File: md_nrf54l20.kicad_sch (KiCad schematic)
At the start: 49 parts, among them J10 Conn_01x15, J2 Conn_01x04, J5 USB_C, J7 JST SH I2C, J9 Conn_01x15, SW1 RESET, U1 nRF54L20, U3 CH347T, U4 AP2112K-3.3, U5 MLD-TF PUSH-H18, Y1 8MHz, Y2 32MHz

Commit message: Fixing Digital mapping
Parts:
- added D6: G_LED, LED_SMD:LED_0402_1005Metric, symbol Device:LED
- added R17: 220, Resistor_SMD:R_0402_1005Metric, symbol Device:R
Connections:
- net +3V3: now also R17.2
- net D10_CS: now also U1.11 (P1.01)
- net D8: now also U1.28 (P0.07)
- net at U1.3 (P2.03): now also D6.1 (K)
- new net: D6.2 (A), R17.1
- no-connect marks 17 -> 18
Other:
- moved on the sheet: C2, C3, C4, C7, C8, R1, R13, R14, R15, R16, SW1, U5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

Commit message: Fixing Digital mapping
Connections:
- net D0_RX: no longer U1.49 (P1.21)
- net D13_SCK: now also U1.26 (P0.04); no longer U1.50 (P1.24)
- net D3_PWM: no longer U1.12 (P1.02)
- net D4: now also U1.3 (P2.03); no longer U1.29 (P0.08)
- net D6_PWM: no longer U1.41 (P1.18)
- net D8: no longer U1.28 (P0.07)
- net at D6.1 (K): no longer U1.3 (P2.03)
- no-connect marks 18 -> 17
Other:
- moved on the sheet: D6, R17
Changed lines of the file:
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@@
 	)
 	(no_connect
-		(at 444.5 217.17)
-	)
-	(no_connect
 		(at 259.08 208.28)
 	)
@@
 	(wire
 		(pts
-			(xy 471.17 240.03) (xy 430.53 240.03)
-		)
-		(stroke
-			(width 0)
-			(type default)
-		)
-	)
-	(wire
-		(pts
 			(xy 383.54 264.16) (xy 394.97 264.16)
 		)
@@
 	(wire
 		(pts
+			(xy 430.53 240.03) (xy 438.15 240.03)
+		)
+		(stroke
+			(width 0)
+			(type default)
+		)
+	)
+	(wire
+		(pts
 			(xy 411.48 144.78) (xy 411.48 208.28)
 		)
@@
 	(wire
 		(pts
-			(xy 485.14 240.03) (xy 478.79 240.03)
+			(xy 505.46 207.01) (xy 499.11 207.01)
 		)
 		(stroke
@@
 		)
 	)
-	(label "D4"
-		(at 448.31 226.06 180)
-		(effects
-			(font
-				(size 1.27 1.27)
-			)
-			(justify right bottom)
-		)
-	)
 	(label "SWDCLK"
 		(at 337.82 306.07 180)
@@
 		)
 	)
-	(label "D3_PWM"
-		(at 379.73 219.71 0)
-		(effects
-			(font
-				(size 1.27 1.27)
-			)
-			(justify left bottom)
-		)
-	)
 	(label "SD_CS"
 		(at 641.35 152.4 0)
@@
 		)
 	)
-	(label "D8"
-		(at 448.31 223.52 180)
+	(label "D0_RX"
+		(at 370.84 243.84 0)
 		(effects
 			(font
 				(size 1.27 1.27)
 			)
-			(justify right bottom)
+			(justify left bottom)
 		)
 	)
@@
 		)
 	)
+	(label "D4"
+		(at 438.15 240.03 180)
+		(effects
+			(font
+				(size 1.27 1.27)
+			)
+			(justify right bottom)
+		)
+	)
 	(label "CH_UART_RX"
 		(at 342.9 298.45 180)
@@
 		)
 	)
+	(label "D8"
+		(at 372.11 257.81 180)
+		(effects
+			(font
+				(size 1.27 1.27)
+			)
+			(justify right bottom)
+		)
+	)
 	(label "A3"
 		(at 383.54 266.7 0)
@@
 		)
 	)
+	(label "D3_PWM"
+		(at 369.57 237.49 0)
+		(effects
+			(font
+				(size 1.27 1.27)
+			)
+			(justify left bottom)
+		)
+	)
 	(label "D2"
 		(at 379.73 237.49 0)
@@
 		)
 	)
+	(label "D6_PWM"
+		(at 363.22 252.73 0)
+		(effects
+			(font
+				(size 1.27 1.27)
+			)
+			(justify left bottom)
+		)
+	)
 	(label "D12_CITO"
 		(at 466.09 349.25 180)
@@
 		)
 	)
-	(label "D6_PWM"
-		(at 379.73 247.65 0)
-		(effects
-			(font
-				(size 1.27 1.27)
-			)
-			(justify left bottom)
-		)
-	)
 	(label "SD_SCK"
 		(at 439.42 234.95 180)
@@
 		)
 	)
-	(label "A6"
-		(at 389.89 336.55 180)
+	(label "D13_SCK"
+		(at 444.5 217.17 180)
 		(effects
 			(font
@@
 		)
 	)
-	(label "D0_RX"
-		(at 372.11 255.27 0)
+	(label "A6"
+		(at 389.89 336.55 180)
 		(effects
 			(font
 				(size 1.27 1.27)
 			)
-			(justify left bottom)
+			(justify right bottom)
 		)
 	)
@@
 		)
 	)
-	(label "D13_SCK"
-		(at 374.65 257.81 0)
-		(effects
-			(font
-				(size 1.27 1.27)
-			)
-			(justify left bottom)
-		)
-	)
 	(label "A6"
 		(at 372.11 227.33 0)
@@
 	(symbol
 		(lib_id "Device:LED")
-		(at 474.98 240.03 0)
+		(at 495.3 207.01 0)
 		(unit 1)
 		(body_style 1)
@@
 		(dnp no)
 		(property "Reference" "D6"
-			(at 473.3925 233.68 0)
+			(at 493.7125 200.66 0)
 			(show_name no)
 			(do_not_autoplace no)
@@
 		)
 		(property "Value" "G_LED"
-			(at 473.3925 236.22 0)
+			(at 493.7125 203.2 0)
 			(show_name no)
 			(do_not_autoplace no)
@@
 		)
 		(property "Footprint" "LED_SMD:LED_0402_1005Metric"
-			(at 474.98 240.03 0)
+			(at 495.3 207.01 0)
 			(hide yes)
 			(show_name no)
@@
 		)
 		(property "Datasheet" ""
-			(at 474.98 240.03 0)
+			(at 495.3 207.01 0)
 			(hide yes)
 			(show_name no)
@@
 		)
 		(property "Description" "Light emitting diode"
-			(at 474.98 240.03 0)
+			(at 495.3 207.01 0)
 			(hide yes)
 			(show_name no)
@@
 		)
 		(property "Sim.Pins" "1=K 2=A"
-			(at 474.98 240.03 0)
+			(at 495.3 207.01 0)
 			(hide yes)
 			(show_name no)
@@
 	(symbol
 		(lib_id "power:+3V3")
-		(at 485.14 232.41 0)
+		(at 505.46 199.39 0)
 		(unit 1)
 		(body_style 1)
@@
 		(dnp no)
 		(property "Reference" "#PWR04"
-			(at 485.14 238.76 0)
+			(at 505.46 205.74 0)
 			(hide yes)
 			(show_name no)
@@
 		)
 		(property "Value" "+3V3"
-			(at 485.14 228.6 0)
+			(at 505.46 195.58 0)
 			(show_name no)
 			(do_not_autoplace no)
@@
 		)
 		(property "Footprint" ""
-			(at 485.14 232.41 0)
+			(at 505.46 199.39 0)
 			(hide yes)
 			(show_name no)
@@
 		)
 		(property "Datasheet" ""
-			(at 485.14 232.41 0)
+			(at 505.46 199.39 0)
 			(hide yes)
 			(show_name no)
@@
 		)
 		(property "Description" ""
-			(at 485.14 232.41 0)
+			(at 505.46 199.39 0)
 			(hide yes)
 			(show_name no)
@@
 	(symbol
 		(lib_id "Device:R")
-		(at 485.14 236.22 0)
+		(at 505.46 203.2 0)
 		(mirror x)
 		(unit 1)
@@
 		(dnp no)
 		(property "Reference" "R17"
-			(at 489.204 237.236 0)
+			(at 509.524 204.216 0)
 			(show_name no)
 			(do_not_autoplace no)
@@
 		)
 		(property "Value" "220"
-			(at 489.458 234.95 0)
+			(at 509.778 201.93 0)
 			(show_name no)
 			(do_not_autoplace no)
@@
 		)
 		(property "Footprint" "Resistor_SMD:R_0402_1005Metric"
-			(at 485.14 236.22 0)
+			(at 505.46 203.2 0)
 			(hide yes)
 			(show_name no)
@@
 		)
 		(property "Datasheet" ""
-			(at 485.14 236.22 0)
+			(at 505.46 203.2 0)
 			(hide yes)
 			(show_name no)
@@
 		)
 		(property "Description" ""
-			(at 485.14 236.22 0)
+			(at 505.46 203.2 0)
 			(hide yes)
 			(show_name no)

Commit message: Routing digital
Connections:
- net D0_RX: now also U1.49 (P1.21)
- net D10_CS: now also U1.29 (P0.08); no longer U1.11 (P1.01)
- net D11_COTI: now also U1.28 (P0.07); no longer U1.23 (P1.08)
- net D12_CITO: now also U1.27 (P0.06); no longer U1.40 (P1.16)
- net D3_PWM: now also U1.12 (P1.02)
- net D6_PWM: now also U1.41 (P1.18)
- net D7: now also U1.40 (P1.16); no longer U1.27 (P0.06)
- net D8: now also U1.39 (P1.15)
- net D9_PWM: now also U1.50 (P1.24); no longer U1.39 (P1.15)
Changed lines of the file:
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@@
+		)
+	)
+	(label "D11_COTI"
+		(at 448.31 223.52 180)
+		(effects
+			(font
+				(size 1.27 1.27)
+			)
+			(justify right bottom)
 		)
 	)
@@
 		)
 	)
-	(label "D9_PWM"
-		(at 379.73 241.3 0)
-		(effects
-			(font
-				(size 1.27 1.27)
-			)
-			(justify left bottom)
-		)
-	)
 	(label "MODE_R"
 		(at 336.55 321.31 180)
@@
 	)
 	(label "D0_RX"
-		(at 370.84 243.84 0)
+		(at 372.11 255.27 0)
+		(effects
+			(font
+				(size 1.27 1.27)
+			)
+			(justify left bottom)
+		)
+	)
+	(label "D7"
+		(at 379.73 243.84 0)
 		(effects
 			(font
@@
 		)
 	)
-	(label "D12_CITO"
-		(at 379.73 243.84 0)
-		(effects
-			(font
-				(size 1.27 1.27)
-			)
-			(justify left bottom)
-		)
-	)
 	(label "A2"
 		(at 405.13 326.39 180)
@@
 		)
 	)
-	(label "D11_COTI"
-		(at 379.73 234.95 0)
-		(effects
-			(font
-				(size 1.27 1.27)
-			)
-			(justify left bottom)
-		)
-	)
 	(label "D5_PWM"
 		(at 466.09 331.47 180)
@@
 		)
 	)
+	(label "D9_PWM"
+		(at 374.65 257.81 0)
+		(effects
+			(font
+				(size 1.27 1.27)
+			)
+			(justify left bottom)
+		)
+	)
 	(label "D8"
-		(at 372.11 257.81 180)
-		(effects
-			(font
-				(size 1.27 1.27)
-			)
-			(justify right bottom)
+		(at 379.73 241.3 0)
+		(effects
+			(font
+				(size 1.27 1.27)
+			)
+			(justify left bottom)
 		)
 	)
@@
 	)
 	(label "D3_PWM"
-		(at 369.57 237.49 0)
+		(at 379.73 219.71 0)
 		(effects
 			(font
@@
 	)
 	(label "D6_PWM"
-		(at 363.22 252.73 0)
+		(at 379.73 247.65 0)
 		(effects
 			(font
@@
 		)
 	)
+	(label "D12_CITO"
+		(at 448.31 220.98 180)
+		(effects
+			(font
+				(size 1.27 1.27)
+			)
+			(justify right bottom)
+		)
+	)
 	(label "SD_SCK"
 		(at 439.42 234.95 180)
@@
 		)
 	)
-	(label "D7"
-		(at 448.31 220.98 180)
+	(label "D10_CS"
+		(at 448.31 226.06 180)
 		(effects
 			(font
@@
 		(effects
 			(font
-				(size 1.27 1.27)
-			)
-			(justify left bottom)
-		)
-	)
-	(label "D10_CS"
-		(at 375.92 217.17 0)
-		(effects
-			(font

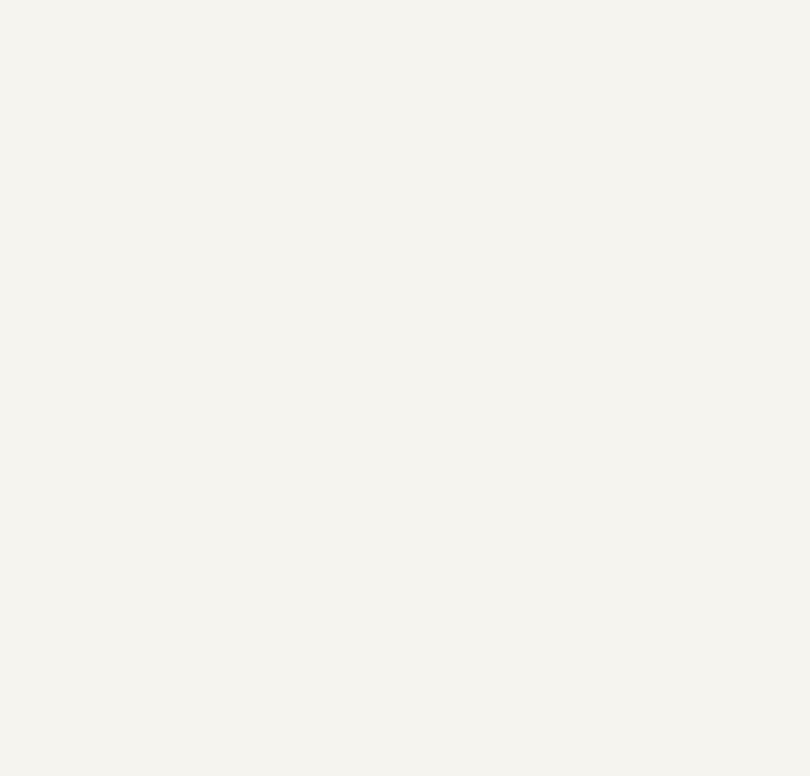
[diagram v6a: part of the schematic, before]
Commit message: Swapping from ch347t to ch347f
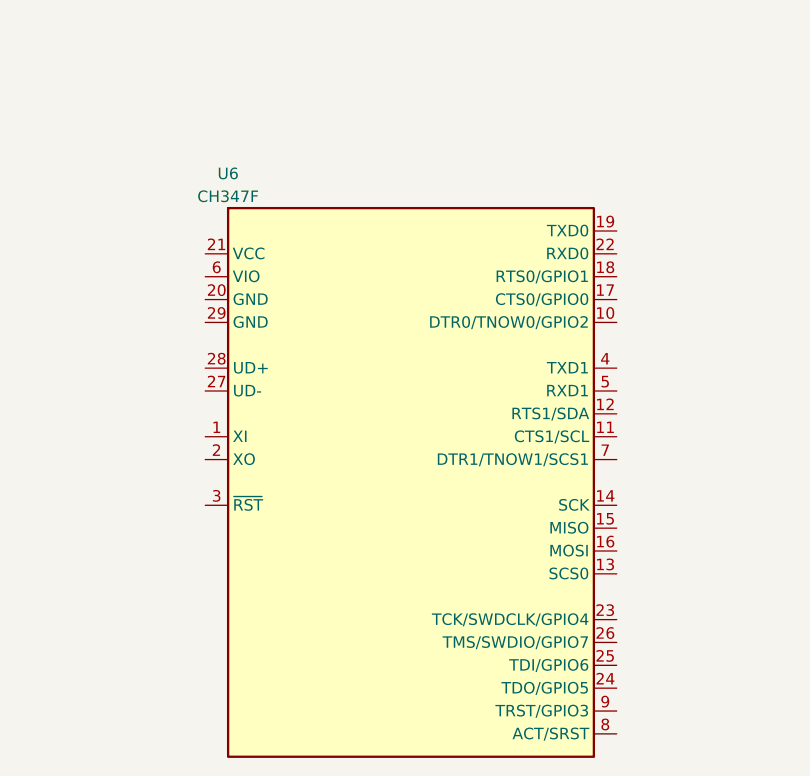
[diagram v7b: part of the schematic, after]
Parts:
- added U6: CH347F, Package_DFN_QFN:QFN-28-1EP_4x4mm_P0.4mm_EP2.4x2.4mm, symbol md_nrf54l20:CH347F
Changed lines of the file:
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@@
+	)
+	(symbol
+		(lib_id "md_nrf54l20:CH347F")
+		(at 300 450 0)
+		(unit 1)
+		(body_style 1)
+		(exclude_from_sim no)
+		(in_bom yes)
+		(on_board yes)
+		(in_pos_files yes)
+		(dnp no)
+		(property "Reference" "U6"
+			(at 279.68 415.71 0)
+			(show_name no)
+			(do_not_autoplace no)
+			(effects
+				(font
+					(size 1.27 1.27)
+				)
+			)
+		)
+		(property "Value" "CH347F"
+			(at 279.68 418.25 0)
+			(show_name no)
+			(do_not_autoplace no)
+			(effects
+				(font
+					(size 1.27 1.27)
+				)
+			)
+		)
+		(property "Footprint" "Package_DFN_QFN:QFN-28-1EP_4x4mm_P0.4mm_EP2.4x2.4mm"
+			(at 300 450 0)
+			(hide yes)
+			(show_name no)
+			(do_not_autoplace no)
+			(effects
+				(font
+					(size 1.27 1.27)
+				)
+			)
+		)
+		(property "Datasheet" "https://www.wch-ic.com/products/CH347.html"
+			(at 300 450 0)
+			(hide yes)
+			(show_name no)
+			(do_not_autoplace no)
+			(effects
+				(font
+					(size 1.27 1.27)
+				)
+			)
+		)
+		(property "Description" "USB high-speed to dual UART/SPI/I2C/JTAG/SWD bridge, QFN-28 4x4mm"
+			(at 300 450 0)
+			(hide yes)
+			(show_name no)
+			(do_not_autoplace no)
+			(effects
+				(font
+					(size 1.27 1.27)
+				)
+			)
+		)
+		(pin "21"
+		)
+		(pin "6"
+		)
+		(pin "20"
+		)
+		(pin "29"
+		)
+		(pin "28"
+		)
+		(pin "27"
+		)
+		(pin "1"
+		)
+		(pin "2"
+		)
+		(pin "3"
+		)
+		(pin "19"
+		)
+		(pin "22"
+		)
+		(pin "18"
+		)
+		(pin "17"
+		)
+		(pin "10"
+		)
+		(pin "4"
+		)
+		(pin "5"
+		)
+		(pin "12"
+		)
+		(pin "11"
+		)
+		(pin "7"
+		)
+		(pin "14"
+		)
+		(pin "15"
+		)
+		(pin "16"
+		)
+		(pin "13"
+		)
+		(pin "23"
+		)
+		(pin "26"
+		)
+		(pin "25"
+		)
+		(pin "24"
+		)
+		(pin "9"
+		)
+		(pin "8"
+		)
+		(instances
+			(project "md_nrf54l20"
+				(path "/66856a8e-a1ed-409f-881b-bdedd4d4f5ae"
+					(reference "U6")
+					(unit 1)
+				)
+			)
+			(project ""
+				(path "/e09869c8-a609-568e-b6fc-992aa2e6349f"
+					(reference "U6")
+					(unit 1)
+				)
+			)
+		)
 	)
 	(symbol

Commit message: Swapping from ch347t to ch347f
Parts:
- removed R10: 10k, Resistor_SMD:R_0402_1005Metric, symbol Device:R
- removed R11, R12: 220, Resistor_SMD:R_0402_1005Metric, symbol Device:R
- removed U3: CH347T, Package_SO:TSSOP-20_4.4x6.5mm_P0.65mm, symbol md_nrf54l20:CH347T
- added C19: 100nF, Capacitor_SMD:C_0402_1005Metric, symbol Device:C
- added D7: G_LED, LED_SMD:LED_0402_1005Metric, symbol Device:LED
- added R10: 4.7k, Resistor_SMD:R_0402_1005Metric, symbol Device:R_US
- added R11, R12: 10k, Resistor_SMD:R_0402_1005Metric, symbol Device:R_US
- added TP1: WCH_RST, TestPoint:TestPoint_Pad_D1.0mm, symbol Connector:TestPoint
- C15: value 1uF -> 100nF
- D5: value O_LED -> G_LED
- R1, R13, R14, R15, R16, R17, R2, R3, R4, R5, R6, R7, R8, R9: symbol Device:R -> Device:R_US
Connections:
- net MODE_D is gone; now on an unnamed net: R9.1
- net USB_DN is gone; now on an unnamed net: J5.A7 (D-), J5.B7 (D-)
- net USB_DP is gone; now on an unnamed net: J5.A6 (D+), J5.B6 (D+)
- net +3V3: now also R9.2, U6.21 (VCC), U6.6 (VIO), R10.1, R11.2, R12.2
- net CH_UART_RX: now also U6.22 (RXD0)
- net CH_UART_TX: now also U6.19 (TXD0), D7.1 (K); no longer D4.1 (K)
- net GND: now also U6.20 (GND), U6.29 (GND), C19.2; no longer R9.2
- net SWDCLK: now also U6.23 (TCK/SWDCLK/GPIO4)
- net SWDIO: now also U6.26 (TMS/SWDIO/GPIO7)
- net nRESET: now also D4.1 (K), U6.8 (ACT/SRST)
- net at U6.1 (XI): now also C12.1, Y1.1
- net at U6.2 (XO): now also C13.1, Y1.3
- net at U6.3 (~{RST}): now also C19.1, R10.2, TP1.1
- net at D5.2 (A): now also R11.1
- new net: D7.2 (A), R12.1
- no-connect marks 17 -> 25
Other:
- moved on the sheet: C11, C12, C13, C14, C15, C17, C18, D1, J5, U4, U6, Y1
